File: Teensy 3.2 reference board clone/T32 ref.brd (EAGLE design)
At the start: 71.1 x 25.4 mm, 89 parts, among them K1 MK20DX256VLH7, K2 MKL04Z32VLC4, P1 LED, T1 MCP1825S - 3.3V, X1 MINI-USB

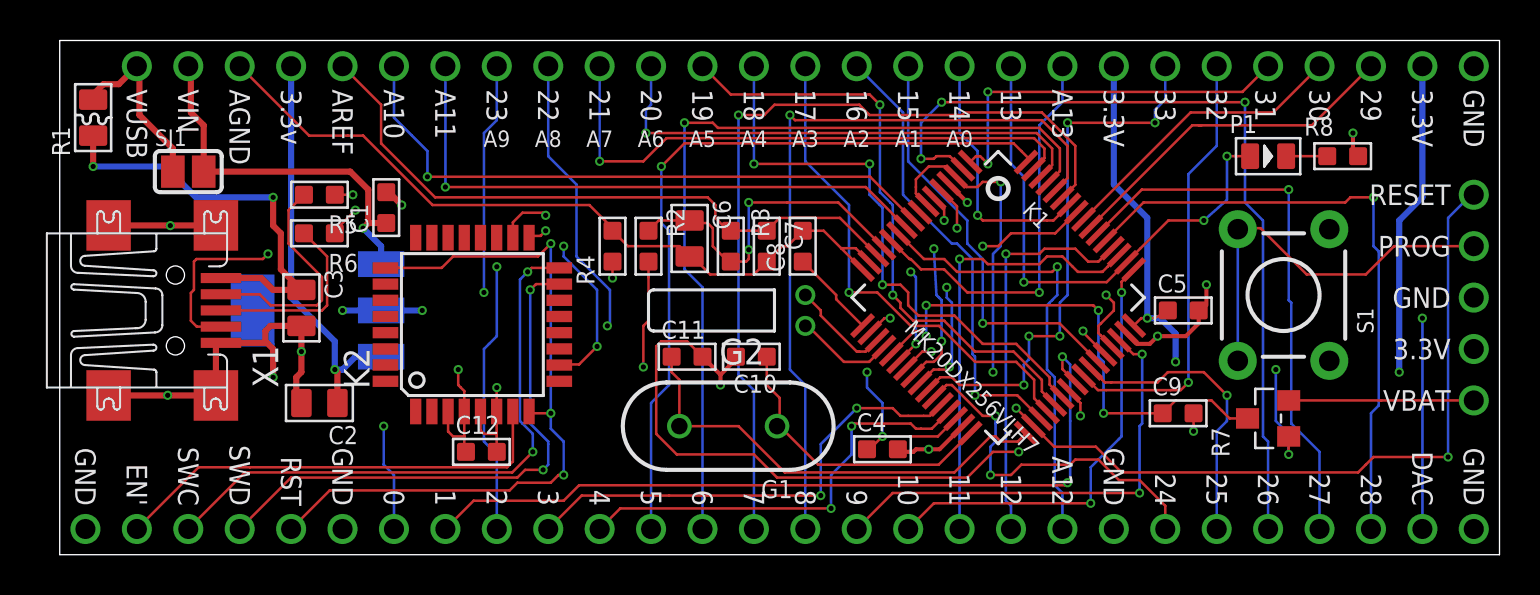
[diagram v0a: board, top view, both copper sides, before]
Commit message: change led and switch, add gerber files for osh park
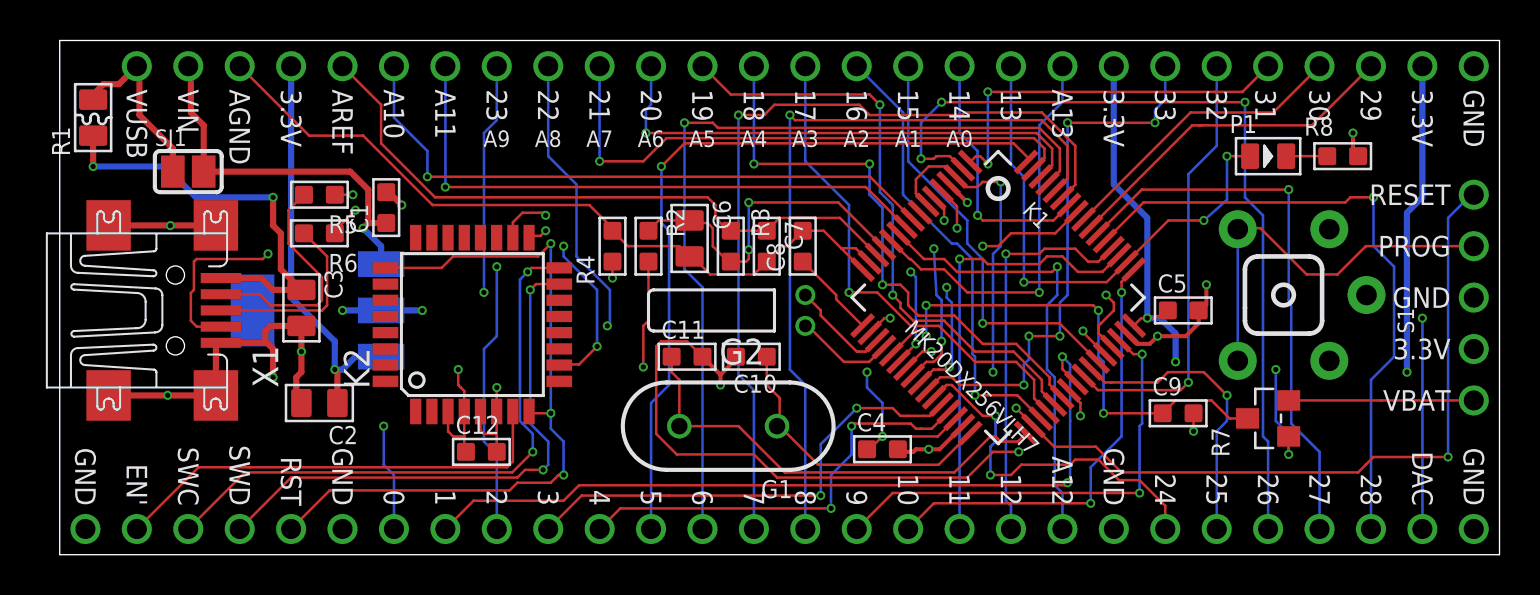
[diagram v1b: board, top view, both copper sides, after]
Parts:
- P1: value LED -> (none)
- S1: device t32_ref:SWITCH_PTH -> t32_ref:ALPS_SKHH
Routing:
- net N$51: track 30.8 -> 31.4 mm
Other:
- board text removed: "3.3v"
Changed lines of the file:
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@@
 <text x="6.35" y="22.987" size="1.016" layer="21" font="vector" ratio="12" rot="SR270" align="center-left">VIN</text>
 <text x="8.89" y="22.987" size="1.016" layer="21" font="vector" ratio="12" rot="SR270" align="center-left">AGND</text>
-<text x="11.43" y="22.987" size="1.016" layer="21" font="vector" ratio="12" rot="SR270" align="center-left">3.3v</text>
+<text x="11.43" y="22.987" size="1.016" layer="21" font="vector" ratio="12" rot="SR270" align="center-left">3.3V</text>
 <text x="13.97" y="22.987" size="1.016" layer="21" font="vector" ratio="12" rot="SR270" align="center-left">AREF</text>
 <text x="16.51" y="22.987" size="1.016" layer="21" font="vector" ratio="12" rot="SR270" align="center-left">A10</text>
@@
 </element>
 <element name="X1" library="t32_ref" package="UX60-MB-5ST" value="MINI-USB" x="5.715" y="12.065">
-<attribute name="OC_NEWARK" value="unknown" x="5.715" y="12.065" size="0.253546875" layer="27" display="off"/>
 <attribute name="MPN" value="UX60-MB-5ST" x="5.715" y="12.065" size="0.253546875" layer="27" display="off"/>
-<attribute name="MF" value="Hirose" x="5.715" y="12.065" size="0.253546875" layer="27" display="off"/>
-<attribute name="OC_FARNELL" value="unknown" x="5.715" y="12.065" size="0.253546875" layer="27" display="off"/>
+<attribute name="MF" value="Hirose Connector" x="5.715" y="12.065" size="0.253546875" layer="27" display="off"/>
 <attribute name="OC_MOUSER" value="798-UX60-MB-5ST" x="5.715" y="12.065" size="1.778" layer="27" display="off"/>
 </element>
@@
 <attribute name="MF" value="NXP Semiconductors" x="59.69" y="6.731" size="1.778" layer="27" rot="R90" display="off"/>
 </element>
-<element name="P1" library="t32_ref" package="LED-0805" value="LED" x="59.69" y="19.685">
-<attribute name="MPN" value="597-3305-607F" x="59.69" y="19.685" size="0.254" layer="27" font="vector" display="off"/>
-<attribute name="OC_MOUSER" value="645-597-3305-607F" x="59.69" y="19.685" size="1.778" layer="27" display="off"/>
-<attribute name="MF" value="Dialight" x="59.69" y="19.685" size="1.778" layer="27" display="off"/>
-</element>
-<element name="S1" library="t32_ref" package="SWITCH_PTH" value="" x="60.452" y="12.827" rot="R90">
-<attribute name="OC_MOUSER" value="688-SKHHAM" x="60.452" y="12.827" size="1.778" layer="27" rot="R90" display="off"/>
-<attribute name="MPN" value="SKHHAMA010" x="60.452" y="12.827" size="1.778" layer="27" rot="R90" display="off"/>
+<element name="P1" library="t32_ref" package="LED-0805" value="" x="59.69" y="19.685">
+<attribute name="MPN" value="SML-211DTT86" x="59.69" y="19.685" size="0.254" layer="27" font="vector" display="off"/>
+<attribute name="OC_MOUSER" value="755-SML-211DTT86" x="59.69" y="19.685" size="1.778" layer="27" display="off"/>
+<attribute name="MF" value="ROHM Semiconductor" x="59.69" y="19.685" size="1.778" layer="27" display="off"/>
+</element>
+<element name="S1" library="t32_ref" package="ALPS_SKHH" value="" x="60.452" y="12.827" rot="R90">
+<attribute name="OC_MOUSER" value="688-SKHHPK" x="60.452" y="12.827" size="1.778" layer="27" rot="R90" display="off"/>
+<attribute name="MPN" value="SKHHPKA010" x="60.452" y="12.827" size="1.778" layer="27" rot="R90" display="off"/>
 <attribute name="MF" value="ALPS" x="60.452" y="12.827" size="1.778" layer="27" rot="R90" display="off"/>
 </element>
@@
 <contactref element="K1" pad="53"/>
 <contactref element="SX43" pad="1"/>
-<wire x1="64.77" y1="1.27" x2="64.77" y2="6.985" width="0.127" layer="16"/>
-<wire x1="64.77" y1="6.985" x2="65.151" y2="7.366" width="0.127" layer="16"/>
-<wire x1="65.151" y1="7.366" x2="65.151" y2="14.986" width="0.127" layer="16"/>
+<wire x1="64.77" y1="1.27" x2="64.77" y2="8.636" width="0.127" layer="16"/>
 <wire x1="65.151" y1="14.986" x2="64.897" y2="15.24" width="0.127" layer="16"/>
 <wire x1="64.897" y1="15.24" x2="64.897" y2="17.653" width="0.127" layer="16"/>
@@
 <wire x1="63.5" y1="17.399" x2="53.53255" y2="17.399" width="0.127" layer="1"/>
 <wire x1="53.53255" y1="17.399" x2="51.6353875" y2="15.5018375" width="0.127" layer="1"/>
+<wire x1="65.151" y1="14.986" x2="65.913" y2="14.224" width="0.127" layer="16"/>
+<wire x1="65.913" y1="14.224" x2="65.913" y2="9.779" width="0.127" layer="16"/>
+<wire x1="65.913" y1="9.779" x2="64.77" y2="8.636" width="0.127" layer="16"/>
 </signal>
 <signal name="N$53">
@@
 <wire x1="41.021" y1="11.684" x2="40.741109375" y2="11.684" width="0.127" layer="1"/>
 <wire x1="40.741109375" y1="11.684" x2="40.0149375" y2="10.957828125" width="0.127" layer="1"/>
-<wire x1="67.31" y1="11.684" x2="59.817" y2="11.684" width="0.127" layer="15"/>
-<wire x1="59.817" y1="11.684" x2="59.309" y2="12.192" width="0.127" layer="15"/>
+<wire x1="67.31" y1="11.684" x2="66.167" y2="11.684" width="0.127" layer="15"/>
+<wire x1="66.167" y1="11.684" x2="65.913" y2="11.43" width="0.127" layer="15"/>
+<wire x1="65.913" y1="11.43" x2="60.071" y2="11.43" width="0.127" layer="15"/>
+<wire x1="60.071" y1="11.43" x2="59.309" y2="12.192" width="0.127" layer="15"/>
 </signal>
 <signal name="N$55">
@@
 <wire x1="59.69" y1="1.27" x2="59.69" y2="5.588" width="0.127" layer="16"/>
 <wire x1="59.69" y1="5.588" x2="59.436" y2="5.842" width="0.127" layer="16"/>
-<wire x1="59.436" y1="5.842" x2="59.436" y2="16.51" width="0.127" layer="16"/>
-<wire x1="59.436" y1="16.51" x2="58.547" y2="17.399" width="0.127" layer="16"/>
-<wire x1="58.547" y1="17.399" x2="58.547" y2="22.352" width="0.127" layer="16"/>
+<wire x1="59.436" y1="5.842" x2="59.436" y2="16.764" width="0.127" layer="16"/>
+<wire x1="59.436" y1="16.764" x2="58.547" y2="17.653" width="0.127" layer="16"/>
+<wire x1="58.547" y1="17.653" x2="58.547" y2="22.352" width="0.127" layer="16"/>
 <via x="58.547" y="22.352" extent="1-16" drill="0.254"/>
 <wire x1="58.547" y1="22.352" x2="43.561" y2="22.352" width="0.127" layer="1"/>
@@
 <contactref element="S1" pad="1"/>
 <contactref element="S1" pad="2"/>
-<wire x1="69.85" y1="15.24" x2="65.913" y2="15.24" width="0.127" layer="1"/>
-<wire x1="65.913" y1="15.24" x2="64.516" y2="13.843" width="0.127" layer="1"/>
-<wire x1="64.516" y1="13.843" x2="61.595" y2="13.843" width="0.127" layer="1"/>
+<wire x1="69.85" y1="15.24" x2="64.516" y2="15.24" width="0.127" layer="1"/>
+<wire x1="64.516" y1="15.24" x2="63.119" y2="13.843" width="0.127" layer="1"/>
+<wire x1="63.119" y1="13.843" x2="61.595" y2="13.843" width="0.127" layer="1"/>
 <wire x1="61.595" y1="13.843" x2="59.309" y2="16.129" width="0.127" layer="1"/>
 <wire x1="59.309" y1="16.129" x2="58.2422" y2="16.129" width="0.127" layer="1"/>
@@
 <wire x1="69.85" y1="10.16" x2="68.326" y2="10.16" width="0.3048" layer="15"/>
 <wire x1="68.326" y1="10.16" x2="67.183" y2="9.017" width="0.3048" layer="15"/>
-<wire x1="67.183" y1="9.017" x2="66.167" y2="9.017" width="0.3048" layer="15"/>
-<via x="66.167" y="9.017" extent="1-16" drill="0.254"/>
-<wire x1="66.167" y1="9.017" x2="66.167" y2="16.51" width="0.3048" layer="16"/>
-<wire x1="66.167" y1="16.51" x2="67.31" y2="17.653" width="0.3048" layer="16"/>
+<wire x1="67.183" y1="9.017" x2="66.548" y2="9.017" width="0.3048" layer="15"/>
+<via x="66.548" y="9.017" extent="1-16" drill="0.254"/>
+<wire x1="66.548" y1="9.017" x2="66.548" y2="16.891" width="0.3048" layer="16"/>
+<wire x1="66.548" y1="16.891" x2="67.31" y2="17.653" width="0.3048" layer="16"/>
 <wire x1="67.31" y1="17.653" x2="67.31" y2="24.13" width="0.3048" layer="16"/>
 <wire x1="60.706" y1="5.842" x2="60.706" y2="4.953" width="0.127" layer="1"/>
@@
 <wire x1="60.071" y1="10.922" x2="63.627" y2="10.922" width="0.3048" layer="15"/>
 <wire x1="63.627" y1="10.922" x2="65.532" y2="9.017" width="0.3048" layer="15"/>
-<wire x1="65.532" y1="9.017" x2="66.167" y2="9.017" width="0.3048" layer="15"/>
+<wire x1="65.532" y1="9.017" x2="66.548" y2="9.017" width="0.3048" layer="15"/>
 <wire x1="56.769" y1="10.668" x2="56.388" y2="10.287" width="0.3048" layer="15"/>
 <via x="55.118" y="9.525" extent="1-16" drill="0.254"/>

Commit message: change usb mini from Hirose to Molex
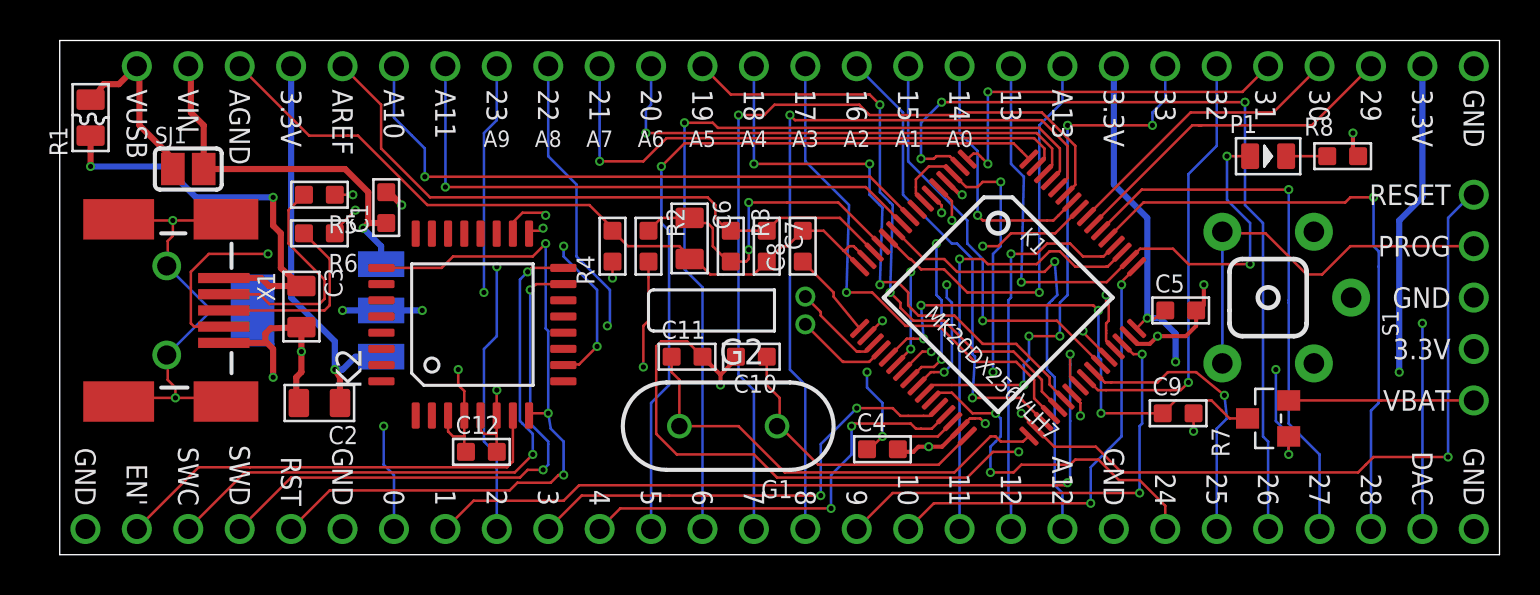
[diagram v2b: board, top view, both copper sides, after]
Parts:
- K1: device t32_ref:QFP50P1200X1200X160-64N -> t32_ref:LQFP64-05
- K2: device t32_ref:TQFP32-08 -> t32_ref:LQFP32-08
- R1: value 0.5A -> FUSE
- R2, R4: value 600R -> (none)
- T1: value MCP1825S - 3.3V -> MCP1825S
- X1: device t32_ref:UX60-MB-5ST -> t32_ref:MOLEX_SD-67503-010
- moved S1 0.77 mm to (59.7, 12.7)
- moved X1 0.43 mm to (5.29, 12.1)
- moved C5 0.13 mm to (55.4, 12.1)
- moved SJ1 0.13 mm to (6.35, 19.1)
- moved R1 0.13 mm to (1.52, 21.6)
- moved C3 0.06 mm to (11.9, 12.3)
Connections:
- net GND: now also X1.P$1, X1.P$2, X1.P$3, X1.P$4, X1.P$5, X1.P$6; no longer X1.M1, X1.M2, X1.M3, X1.M4
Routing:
- net GND: track 81.5 -> 92.2 mm, vias 17 -> 18
- net N$31: track 25.9 -> 30.2 mm
- net N$3: track 27.7 -> 28.6 mm
- net N$51: track 31.4 -> 30.6 mm
- net N$9: track 57.2 -> 56.6 mm
- net N$10: track 34.3 -> 33.8 mm
